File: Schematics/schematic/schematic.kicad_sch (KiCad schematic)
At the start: 35 parts, among them U1 ESP32-WROOM-32D, U2 74HC595-IC, U3 74HC595-IC

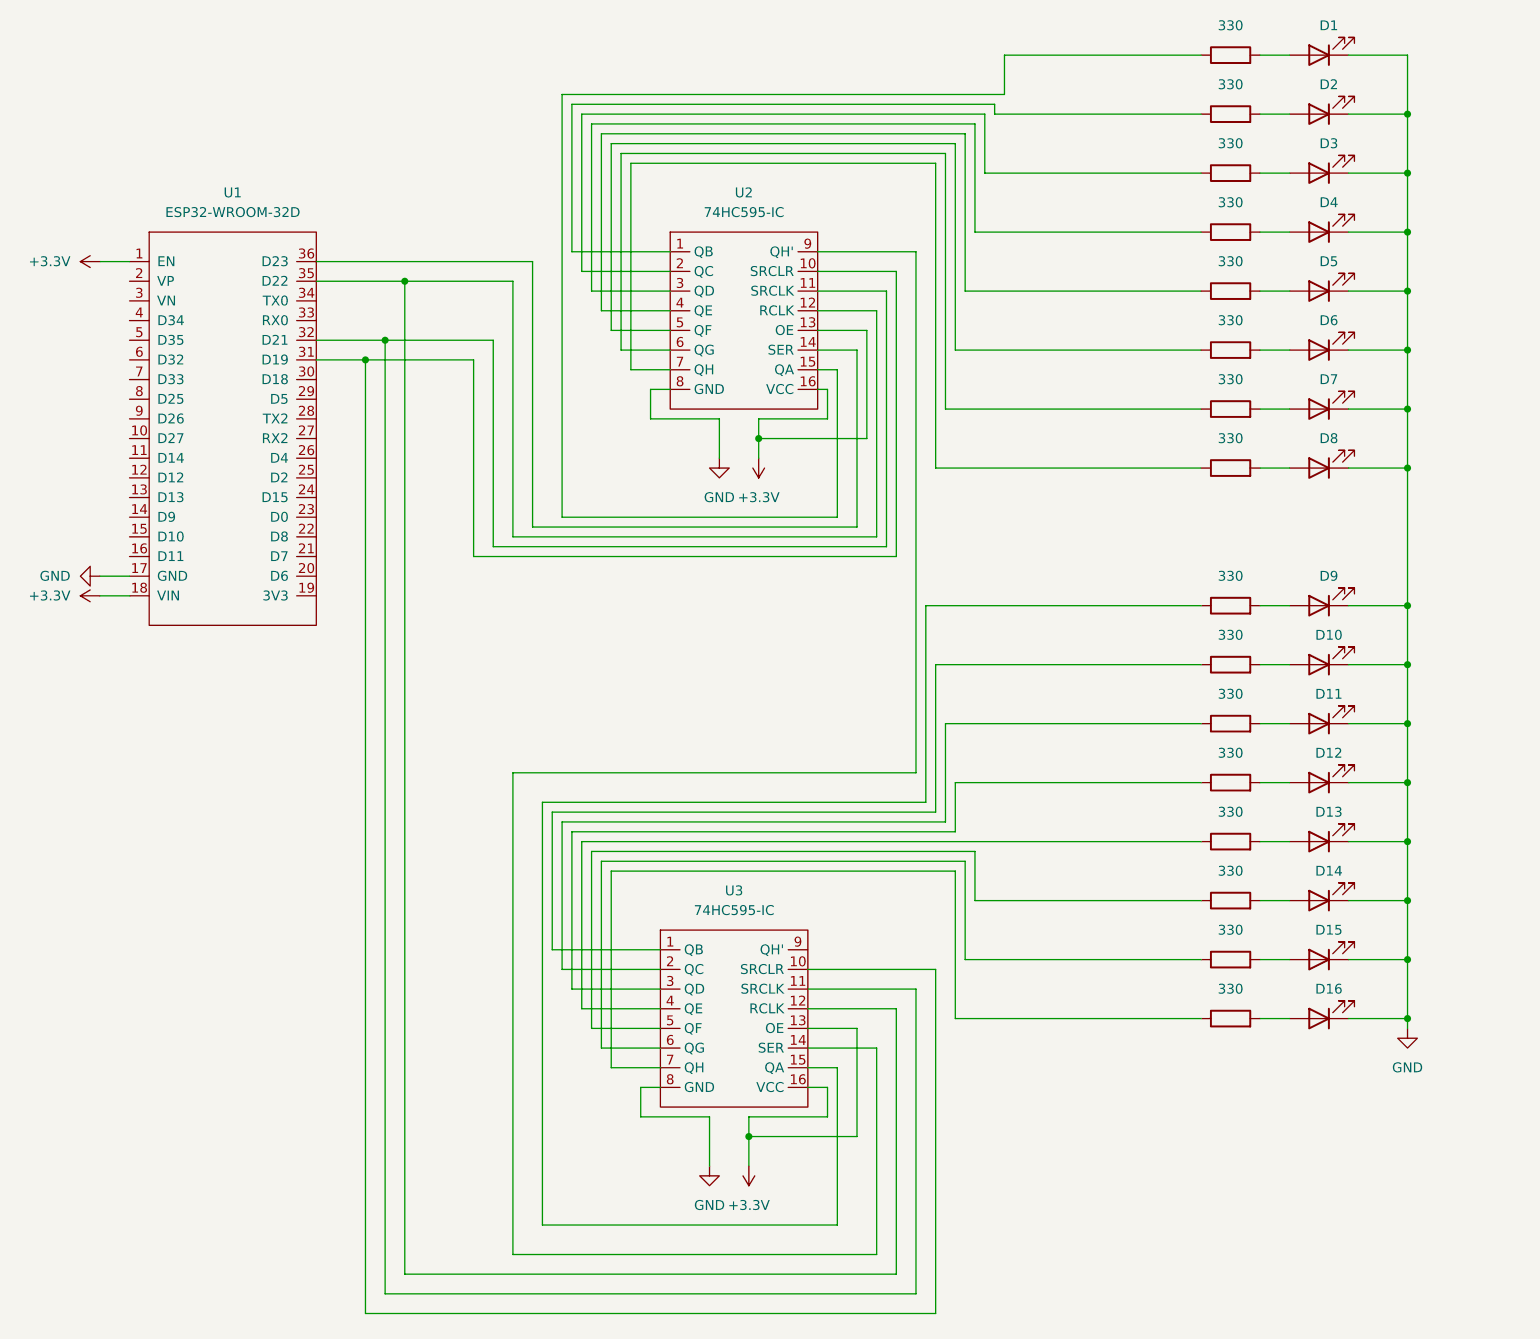
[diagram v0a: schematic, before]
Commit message: updated schematic symbols, uploaded code to power 74hc595
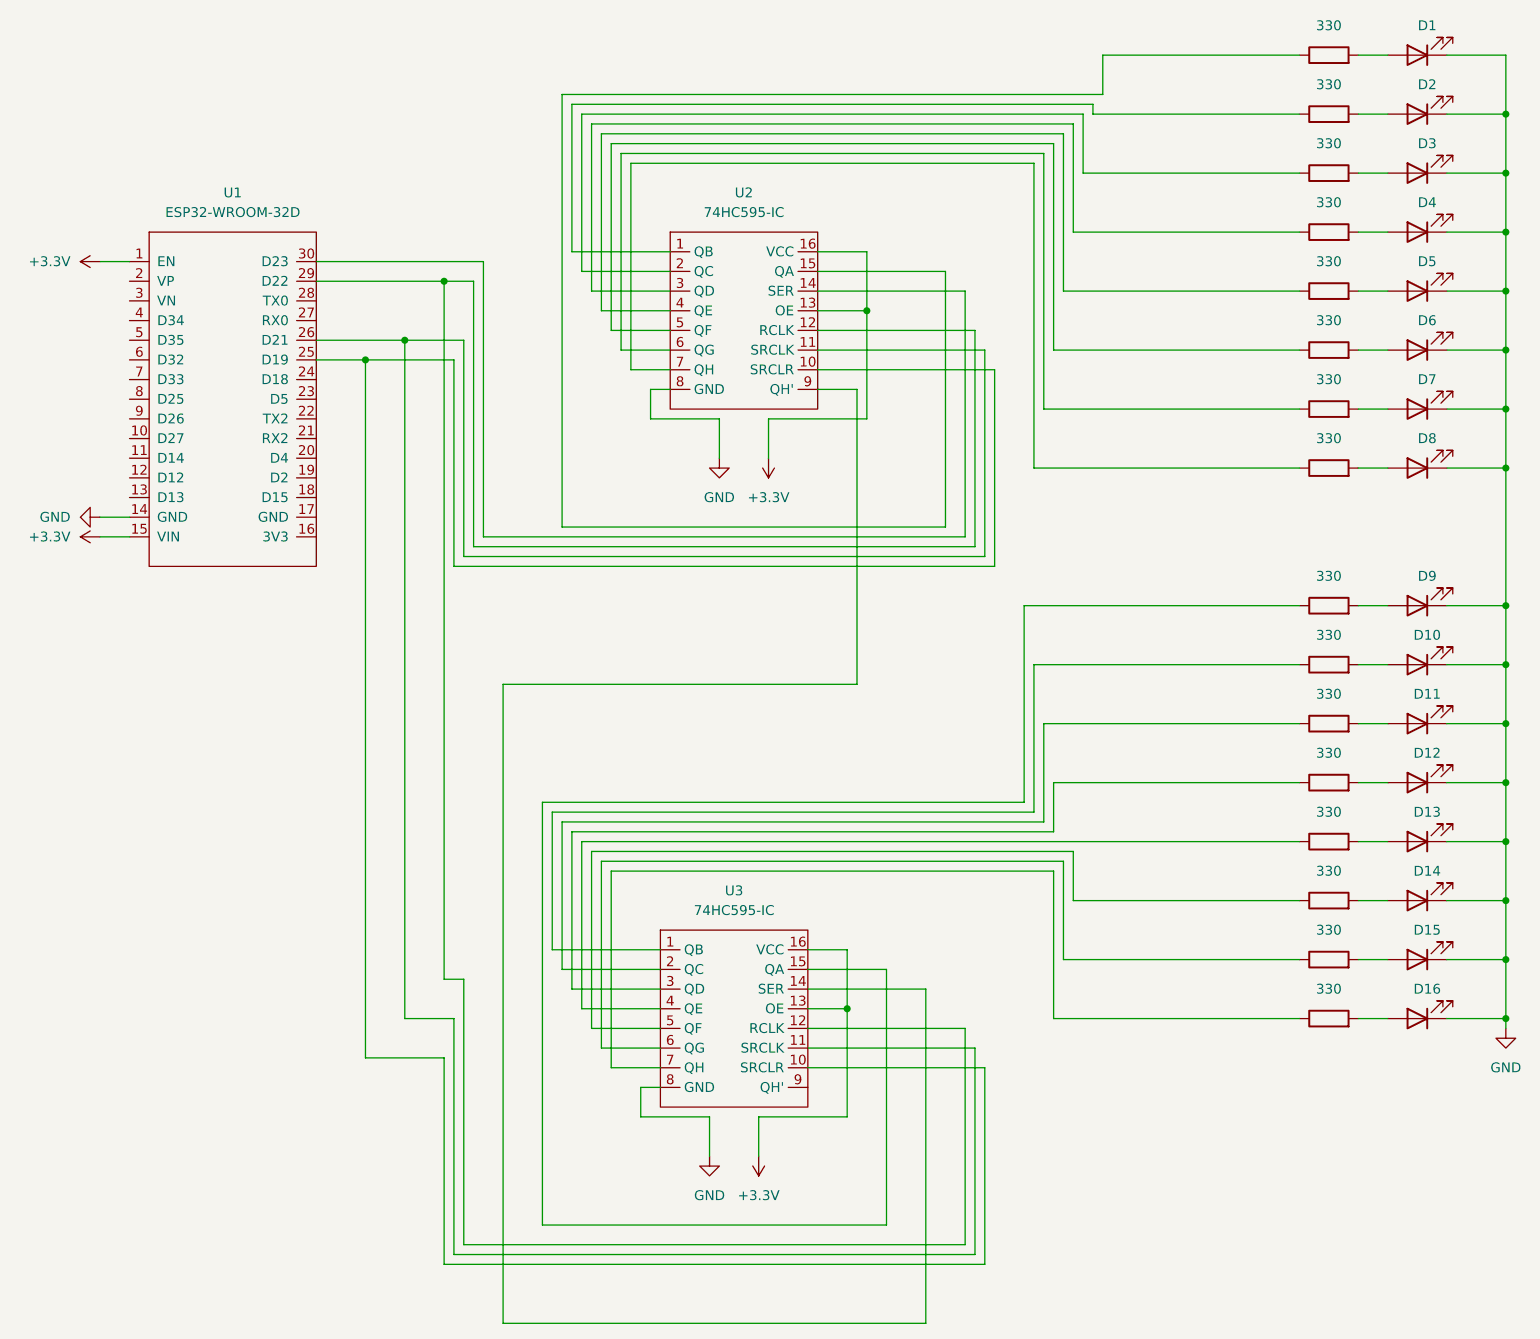
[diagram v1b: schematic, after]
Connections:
- net +3.3V: now also U1.15 (VIN); no longer U1.18 (VIN)
- net GND: now also U1.14 (GND); no longer U1.17 (GND)
- net at U1.25 (D19): now also U2.10 (SRCLR), U3.10 (SRCLR)
- net at U1.26 (D21): now also U2.11 (SRCLK), U3.11 (SRCLK)
- net at U1.29 (D22): now also U2.12 (RCLK), U3.12 (RCLK)
- net at U1.30 (D23): now also U2.14 (SER)
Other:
- moved on the sheet: D1, D10, D11, D12, D13, D14, D15, D16, D2, D3, D4, D5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

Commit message: added colored wires
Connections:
- net +3.3V: no longer U2.13 (OE), U3.13 (OE)
- net GND: now also U2.13 (OE), U3.13 (OE)
